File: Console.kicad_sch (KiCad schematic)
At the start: 17 parts

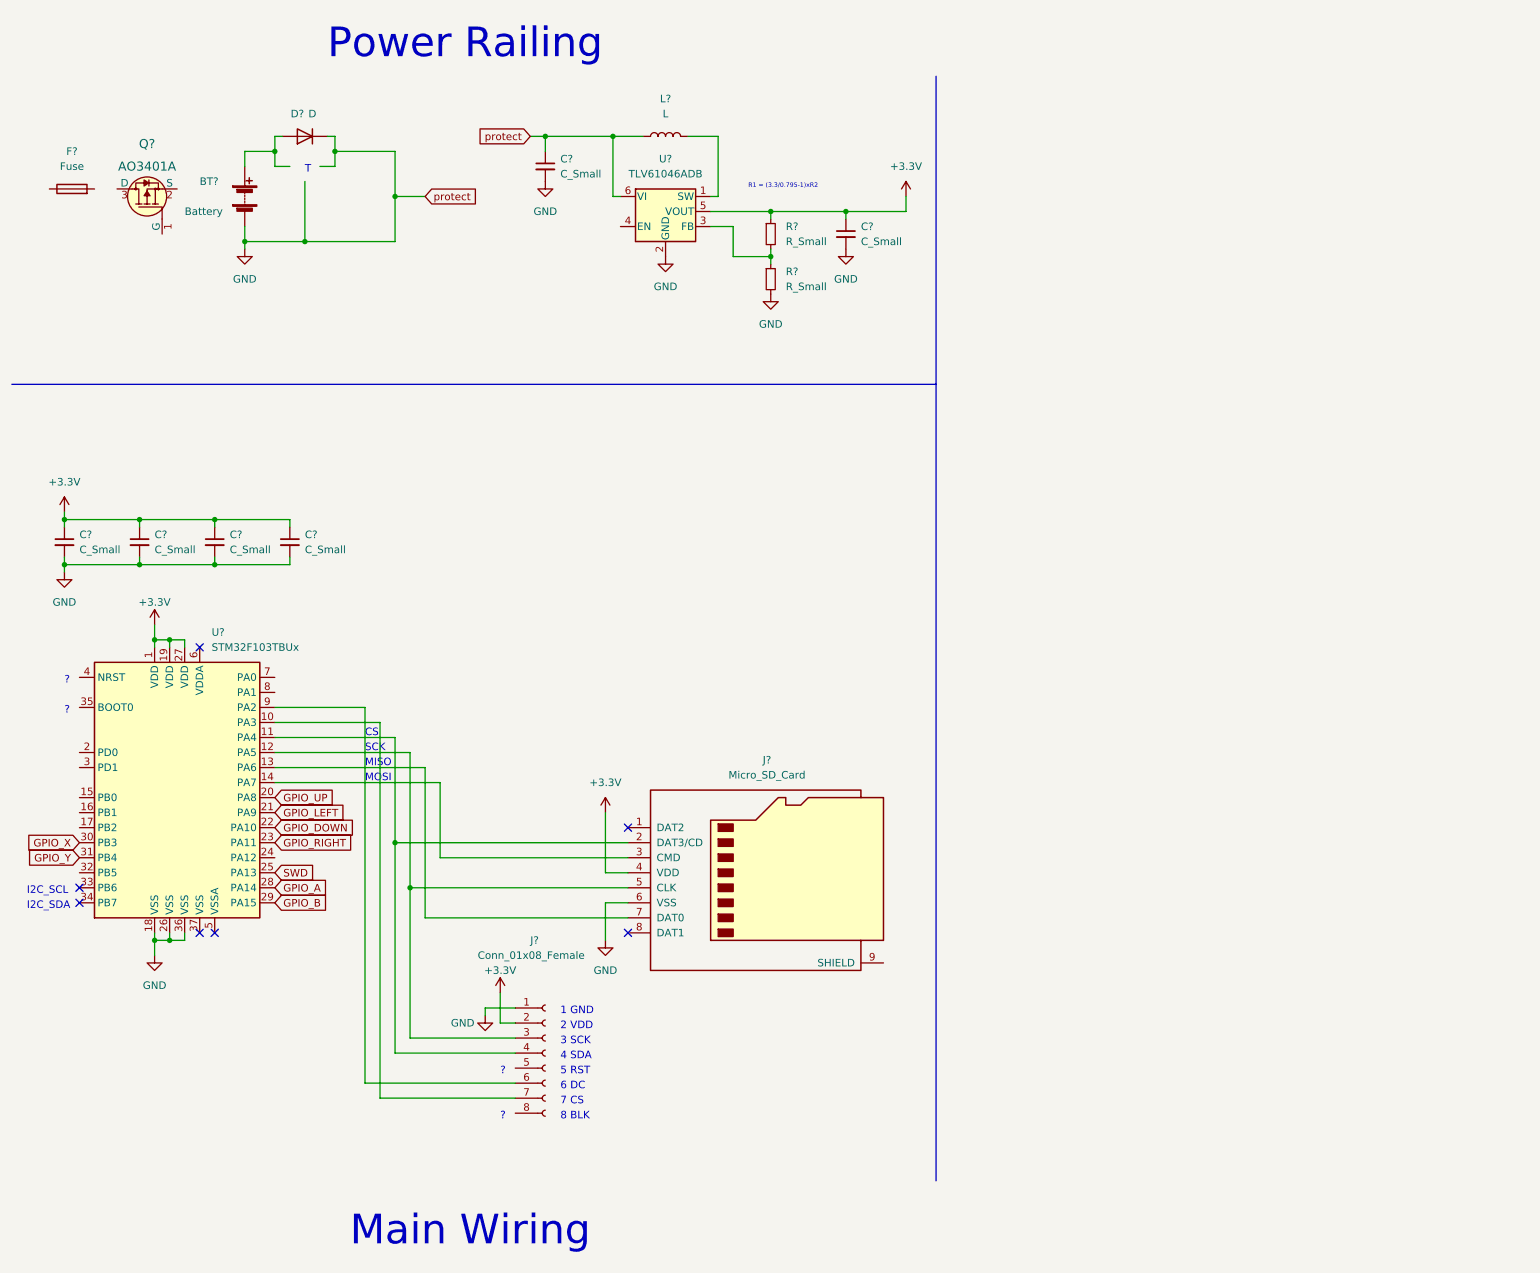
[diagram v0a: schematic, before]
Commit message: changed the power railing, switched the boost converter with LDO
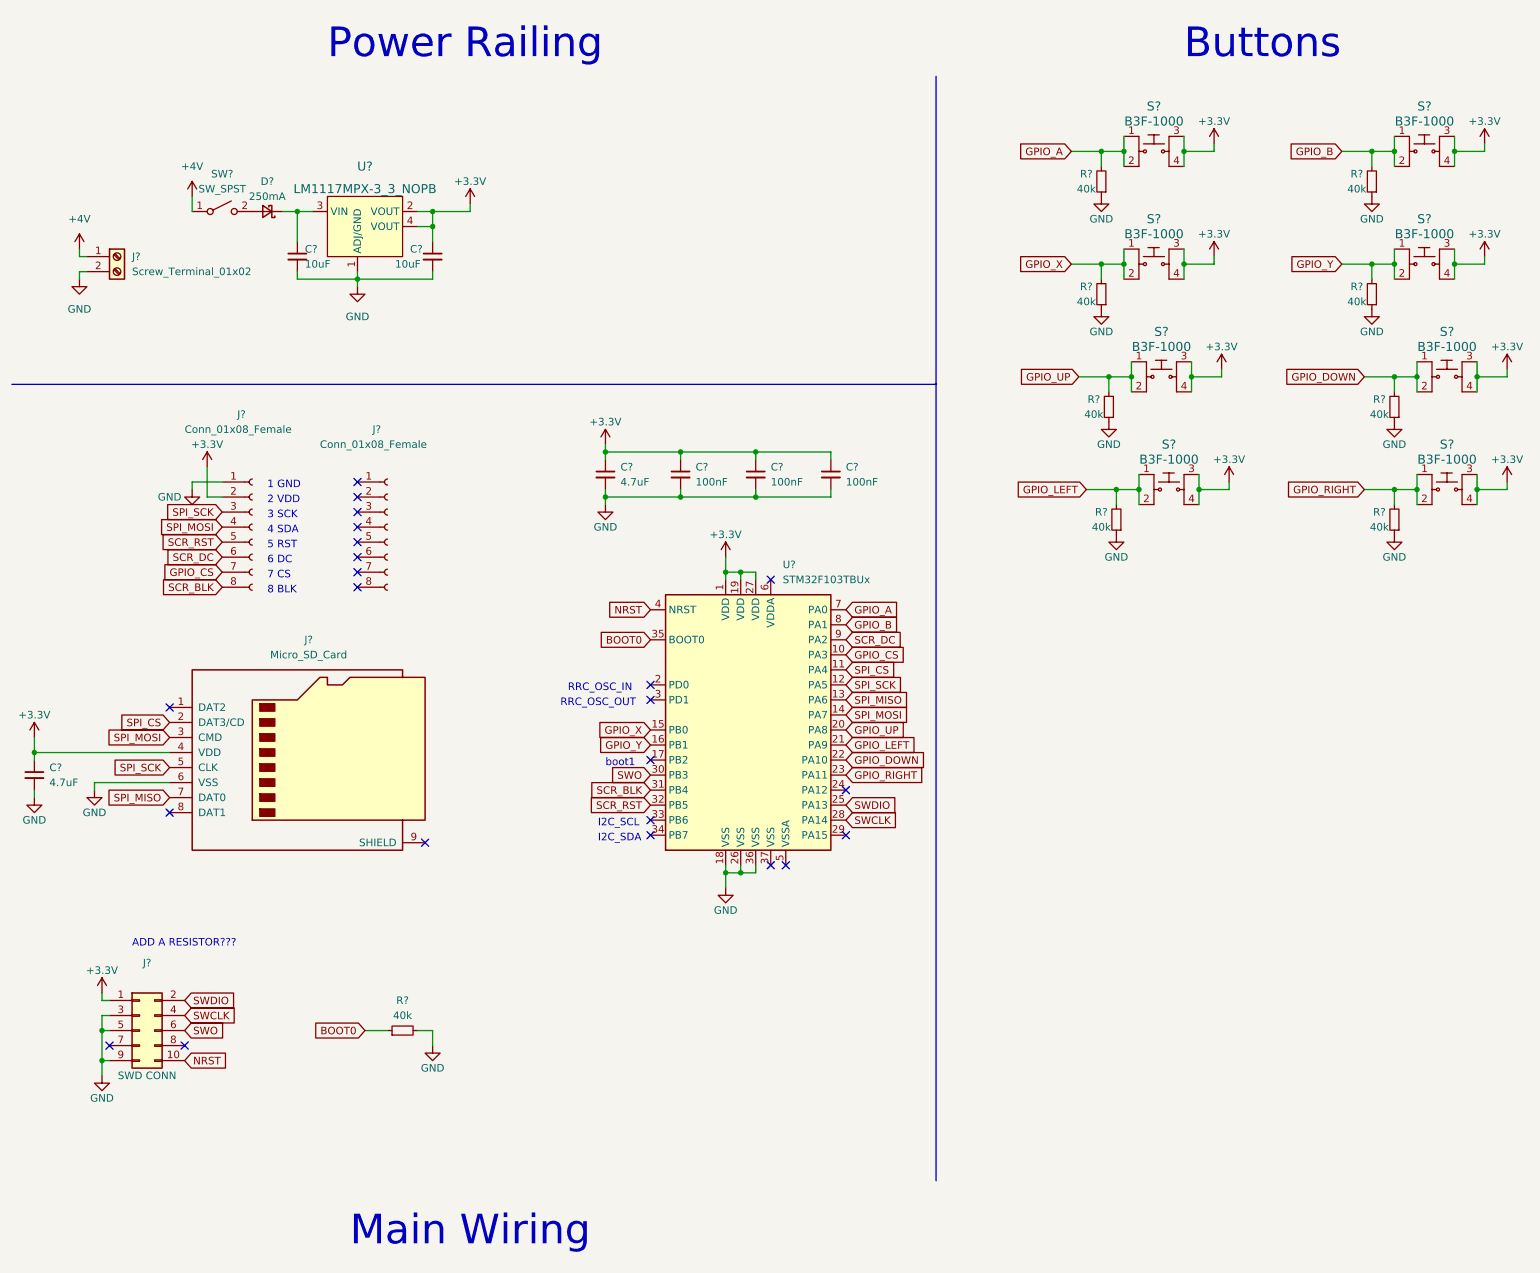
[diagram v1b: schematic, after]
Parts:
- removed BT?: Battery, symbol Device:Battery
- removed C? (x2): C_Small, symbol Device:C_Small
- removed D?: D, symbol Device:D
- removed F?: Fuse, symbol Device:Fuse
- removed L?: L, symbol Device:L
- removed Q?: AO3401A, digikey-footprints:SOT-23-3, symbol dk_Transistors-FETs-MOSFETs-Single:AO3401A
- removed R? (x2): R_Small, symbol Device:R_Small
- removed U?: TLV61046ADB, Package_TO_SOT_SMD:SOT-23-6, symbol Regulator_Switching:TLV61046ADB
- added C? (x2): 10uF, symbol Device:C_Small
- added C?: 4.7uF, symbol Device:C_Small
- added D?: 250mA, symbol Device:D_Schottky_Small
- added J?: Conn_01x08_Female, Connector_PinHeader_2.54mm:PinHeader_1x08_P2.54mm_Vertical, symbol Connector:Conn_01x08_Female
- added J?: Screw_Terminal_01x02, symbol Connector:Screw_Terminal_01x02
- added J?: SWD CONN, symbol Connector_Generic:Conn_02x05_Odd_Even
- added R? (x9): 40k, symbol Device:R_Small
- added S? (x8): B3F-1000, digikey-footprints:Switch_Tactile_THT_B3F-1xxx, symbol dk_Tactile-Switches:B3F-1000
- added SW?: SW_SPST, symbol Switch:SW_SPST
- added U?: LM1117MPX-3_3_NOPB, digikey-footprints:SOT-223, symbol dk_PMIC-Voltage-Regulators-Linear:LM1117MPX-3_3_NOPB
- C? (x3): value C_Small -> 100nF
- C?: value C_Small -> 4.7uF
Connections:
- net +3.3V: now also C?.1, C?.1, J?.1 (Pin_1), S?.3, S?.3, S?.3, S?.3, S?.3, S?.3, S?.3, S?.3, S?.4, S?.4, S?.4, S?.4, S?.4, S?.4, S?.4, S?.4, U?.2 (VOUT), U?.4 (VOUT)
- net GND: now also C?.2, C?.2, C?.2, J?.2 (Pin_2), J?.3 (Pin_3), J?.5 (Pin_5), J?.9 (Pin_9), R?.1, R?.1, R?.1, R?.1, R?.1, R?.1, R?.1, R?.1, R?.2, U?.1 (ADJ/GND)
- net GPIO_A: now also U?.7 (PA0), R?.2, S?.1, S?.2; no longer U?.28 (PA14)
- net GPIO_B: now also U?.8 (PA1), R?.2, S?.1, S?.2; no longer U?.29 (PA15)
- net GPIO_DOWN: now also R?.2, S?.1, S?.2
- net GPIO_LEFT: now also R?.2, S?.1, S?.2
- net GPIO_RIGHT: now also R?.2, S?.1, S?.2
- net GPIO_UP: now also R?.2, S?.1, S?.2
- net GPIO_X: now also U?.15 (PB0), R?.2, S?.1, S?.2; no longer U?.30 (PB3)
- net GPIO_Y: now also U?.16 (PB1), R?.2, S?.1, S?.2; no longer U?.31 (PB4)
- net SPI_SCK: now reaches J?.3 (Pin_3), J?.5 (CLK), U?.12 (PA5)
- net SPI_CS: now reaches J?.2 (DAT3/CD), U?.11 (PA4)
- net SPI_CS: no longer J?.4 (Pin_4)
- net SCR_RST: now reaches J?.5 (Pin_5)
- net SCR_RST: now also U?.32 (PB5)
- net SCR_DC: now reaches J?.6 (Pin_6), U?.9 (PA2)
- net GPIO_CS: now reaches J?.7 (Pin_7), U?.10 (PA3)
- net SCR_BLK: now reaches J?.8 (Pin_8)
- net SCR_BLK: now also U?.31 (PB4)
- net SPI_MOSI: now reaches J?.3 (CMD), U?.14 (PA7)
- net SPI_MOSI: now also J?.4 (Pin_4)
- net SPI_MISO: now reaches J?.7 (DAT0), U?.13 (PA6)
- net BOOT0: now reaches U?.35 (BOOT0)
- net BOOT0: now also R?.1
- net NRST: now reaches U?.4 (NRST)
- net NRST: now also J?.10 (Pin_10)
- net SWD renamed SWDIO
- net SWDIO: now also J?.2 (Pin_2)
- new net: D?.2 (A), SW?.2 (B)
- new net: C?.1, D?.1 (K), U?.3 (VIN)
- new net +4V: J?.1 (Pin_1), SW?.1 (A)
- new net SWCLK: J?.4 (Pin_4), U?.28 (PA14)
- new net SWO: J?.6 (Pin_6), U?.30 (PB3)
- no-connect marks 7 -> 23
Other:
- note added: "ADD A RESISTOR???"
- note added: "Buttons"
- note added: "RRC_OSC_IN"
- note added: "RRC_OSC_OUT"
- note added: "boot1"
- note removed: "?"
- note removed: "CS"
- note removed: "MISO"
- note removed: "MOSI"
- note removed: "R1 = (3.3/0.795-1)xR2"
- note removed: "SCK"
- note removed: "T"
- moved on the sheet: C?, J?, U?

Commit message: sorted power rails, assigned footprints etc
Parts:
- removed J?: Screw_Terminal_01x02, symbol Connector:Screw_Terminal_01x02
- removed SW?: SW_SPST, symbol Switch:SW_SPST
- added C2: 4.7uF, symbol Device:C_Small
- added J4: USB_B_Micro, Connector_USB:USB_Micro-B_Molex-105017-0001, symbol Connector:USB_B_Micro
- gave numbers to parts that had none: 31
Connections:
- net +3.3V: now also J2.1 (Pin_1), C2.2; no longer J2.2 (Pin_2), U1.4 (VOUT)
- net GND: now also J2.2 (Pin_2), C2.1, J4.5 (GND), J4.6 (Shield); no longer J2.1 (Pin_1)
- net +5V: now reaches D1.2 (A)
- net +5V: now also J4.1 (VBUS)
- no-connect marks 23 -> 27
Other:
- moved on the sheet: C3, C5, D1, U1

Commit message: final commit (hopefully) for V01
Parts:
- added H1, H2, H3, H4: MountingHole_Pad, MountingHole:MountingHole_4.3mm_M4_Pad_Via, symbol Mechanical:MountingHole_Pad
- C1, C2, C4: footprint (none) -> Capacitor_SMD:C_0805_2012Metric; Cxx (none) -> Cxxxx; LCSC Part # (none) -> C1779
- C3, C5: footprint (none) -> Capacitor_SMD:C_1206_3216Metric; Cxx (none) -> Cxxxx; LCSC Part # (none) -> C13585
- C6, C7, C8: footprint (none) -> Capacitor_SMD:C_0402_1005Metric; Cxx (none) -> Cxxxx; LCSC Part # (none) -> C24497
- D1: value 250mA -> 600mA; footprint (none) -> Diode_SMD:D_SOD-323; Cxx (none) -> Cxxxx; LCSC Part # (none) -> C191023
- J1: footprint (none) -> Connector_PinHeader_1.27mm:PinHeader_2x05_P1.27mm_Vertical_SMD; Cxx (none) -> Cxxxx; LCSC Part # (none) -> C2881910
- J2, J5: footprint Connector_PinHeader_2.54mm:PinHeader_1x08_P2.54mm_Vertical -> Connector_PinSocket_2.54mm:PinSocket_1x08_P2.54mm_Vertical
- J3: footprint (none) -> libraries:microSD_HC_Molex_104031-0811; Cxx (none) -> Cxxxx; LCSC Part # (none) -> C585350
- J4: footprint Connector_USB:USB_Micro-B_Molex-105017-0001 -> Connector_USB:USB_Micro-B_Molex-105133-0001; Cxx (none) -> Cxxxx; LCSC Part # (none) -> C782257
- R1, R2, R3, R4, R5, R6, R7, R8, R9: value 40k -> 24k; footprint (none) -> Resistor_SMD:R_0805_2012Metric; Cxx (none) -> Cxxxx; LCSC Part # (none) -> C17575
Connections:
- net GND: now also J3.9 (SHIELD), H1.1, H2.1, H3.1, H4.1
- no-connect marks 27 -> 26
